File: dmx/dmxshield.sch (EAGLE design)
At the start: 17 parts, among them IC1 MAX3468CPA, X1 NC5FAV

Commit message: use on board IC
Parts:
- removed SV1: (no value), con-dil:IC16E
- added SV2: (no value), con-lstb:MA04-2
- IC1: value MAX3468CPA -> MAX3468CSA; device maxim:MAX3468CPA -> maxim:MAX3468CSA; MPN (none) -> MAX3468CSA+; OC_NEWARK (none) -> 76K6721
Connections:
- removed net N$12: C1.1, DC1.+VOUT1, IC1.VCC, OK1.A, OK2.VCC, OK3.VCC, R8.1, R9.1
- removed net N$17: C1.2, DC1.-VOUT1, OK2.GND, OK3.GND, R1.1, X1.1, X1.G
- removed net N$7: R5.1, SV1-11.S
- new net GND: C1.2, DC1.-VIN1, DC1.-VOUT1, IC1.GND, OK1.GND, OK2.GND, OK3.GND, R1.1, SV2.8, X1.1, X1.G
- new net N$3: R5.1, SV2.5
- new net VCC: C1.1, DC1.+VIN1, DC1.+VOUT1, IC1.VCC, OK1.A, OK2.VCC, OK3.VCC, R8.1, R9.1, SV2.4
- net N$1: now also SV2.7; no longer SV1-9.S
- net N$16: now also R6.1, SV2.3; no longer DC1.-VIN1, OK1.GND, SV1-1.S
- net N$5: no longer DC1.+VIN1, SV1-4.S
- net N$6: now also LED1.A; no longer R6.1, SV1-10.S
- net N$8: no longer LED1.A
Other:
- note removed: "5V"
- note removed: "DATA"
- note removed: "GND"
- note removed: "RX"
- note removed: "TX"
- moved on the sheet: R2, X1

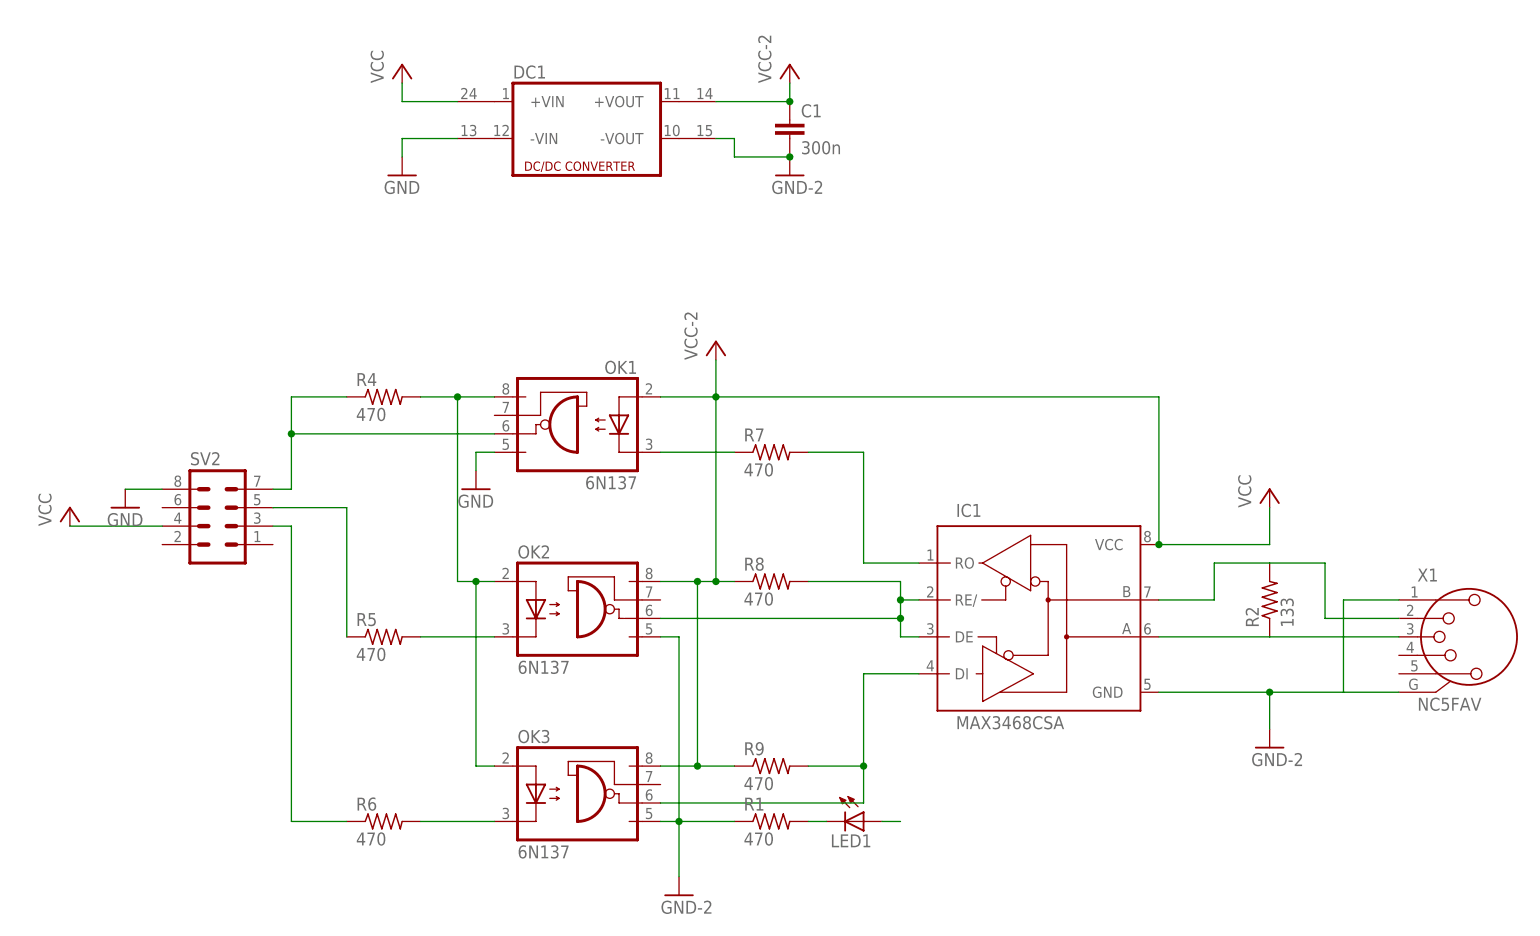
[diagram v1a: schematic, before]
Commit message: change all components to surface mounted
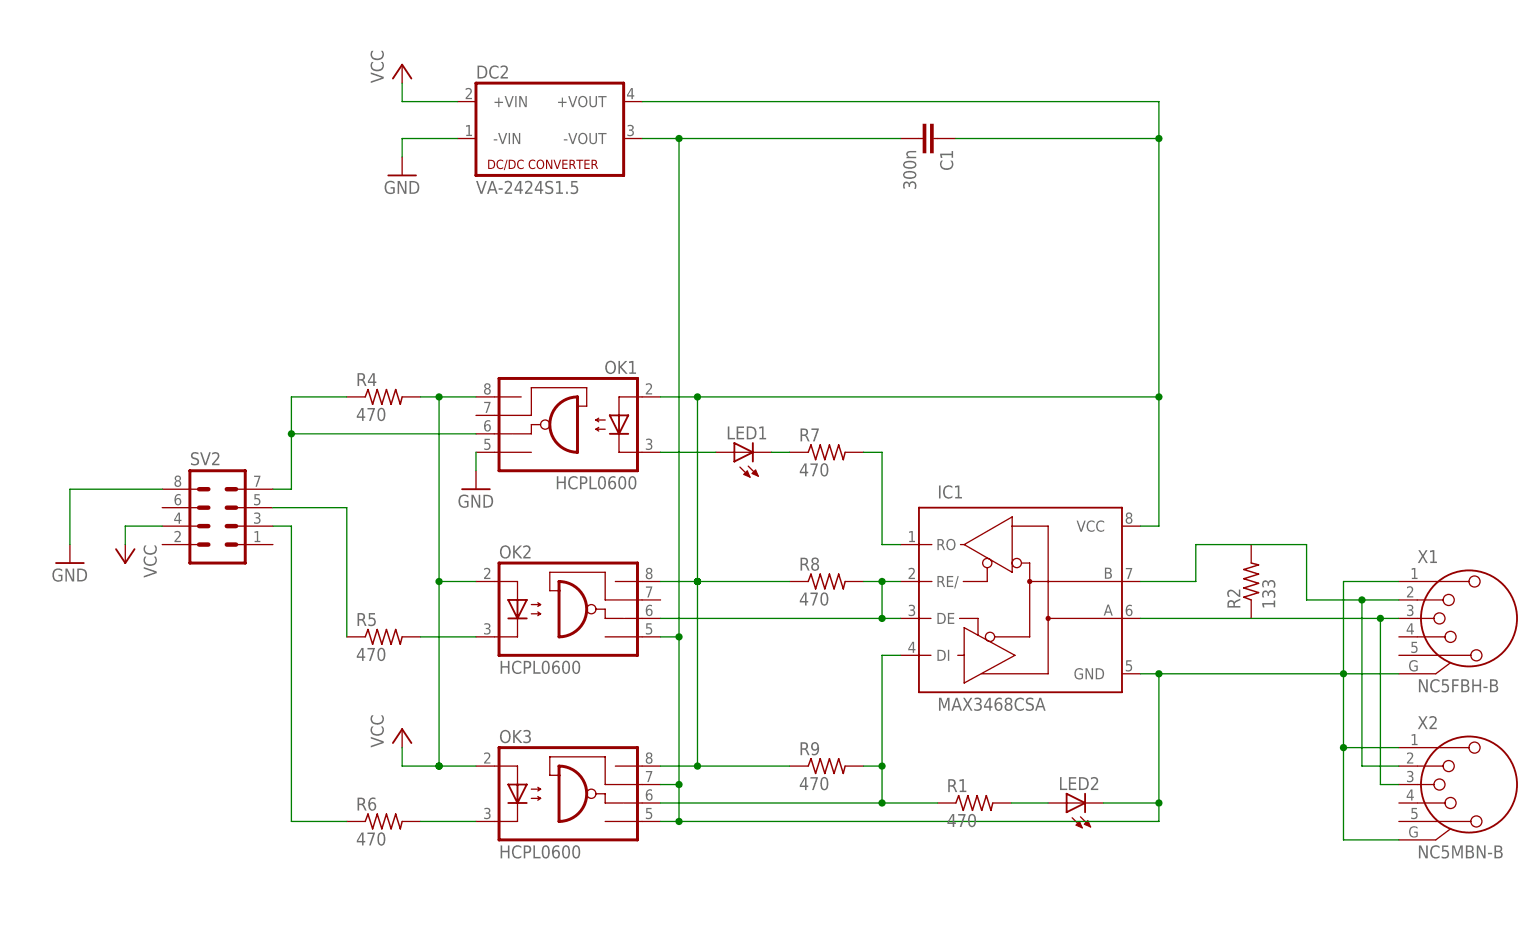
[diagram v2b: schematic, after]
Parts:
- removed DC1: (no value), dc-dc-converter:DCW1U
- added DC2: VA-2424S1.5, dc-dc-converter:VA-2424S1.5
- added LED2: (no value), led:LEDCHIP-LED0805
- added X2: NC5MBN-B, con-neutrik_ag:NC5MBN-B
- C1: device capacitor-wima:C5/3 -> resistor:C-EUC0805
- LED1: device led:LED3MM -> led:LEDCHIP-LED0805
- OK1, OK2, OK3: value 6N137 -> HCPL0600; device optocoupler:6N137 -> optocoupler:HCPL0600; MF (none) -> AGILENT TECHNOLOGIES; MPN (none) -> HCPL-0600-000E; OC_FARNELL (none) -> 9994696; OC_NEWARK (none) -> 88H7774
- R1, R2, R4, R5, R6, R7, R8, R9: device resistor:R-US_0204/7 -> resistor:R-US_R0805
- X1: value NC5FAV -> NC5FBH-B; device con-neutrik_ag:NC5FAV -> con-neutrik_ag:NC5FBH-B; OC_NEWARK (none) -> unknown
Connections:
- new net N$7: C1.2, DC2.-VOUT, IC1.GND, LED2.C, OK2.GND, OK3.GND, OK3.VE, X1.1, X1.G, X2.1, X2.G
- net GND: now also DC2.-VIN; no longer C1.2, DC1.-VIN1, DC1.-VOUT1, IC1.GND, OK2.GND, OK3.GND, R1.1, X1.1, X1.G
- net N$11: now also LED2.A; no longer LED1.C
- net N$13: now also R1.1
- net N$14: now also X2.2
- net N$15: now also X2.3
- net N$5: now also LED1.A, OK1.C; no longer OK1.VCC, OK2.A, OK3.A, R4.2
- net N$6: now also C1.1, DC2.+VOUT, IC1.VCC, OK1.A, OK2.VCC, OK3.VCC, R8.1, R9.1; no longer LED1.A
- net N$9: now also LED1.C; no longer OK1.C
- net VCC: now also DC2.+VIN, OK1.VCC, OK2.A, OK3.A, R4.2; no longer C1.1, DC1.+VIN1, DC1.+VOUT1, IC1.VCC, OK1.A, OK2.VCC, OK3.VCC, R8.1, R9.1
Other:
- moved on the sheet: C1, IC1, LED1, OK1, OK2, OK3, R1, R2, R7, R8, R9, X1
